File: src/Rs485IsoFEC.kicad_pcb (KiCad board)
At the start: 2 copper layers, 24 x 27.9 mm, 28 parts, among them J1 B4B-XH-A, P1 105444-0001, Q1 DMP3099L-13, U1 FT232RL, U2 ADM2682E

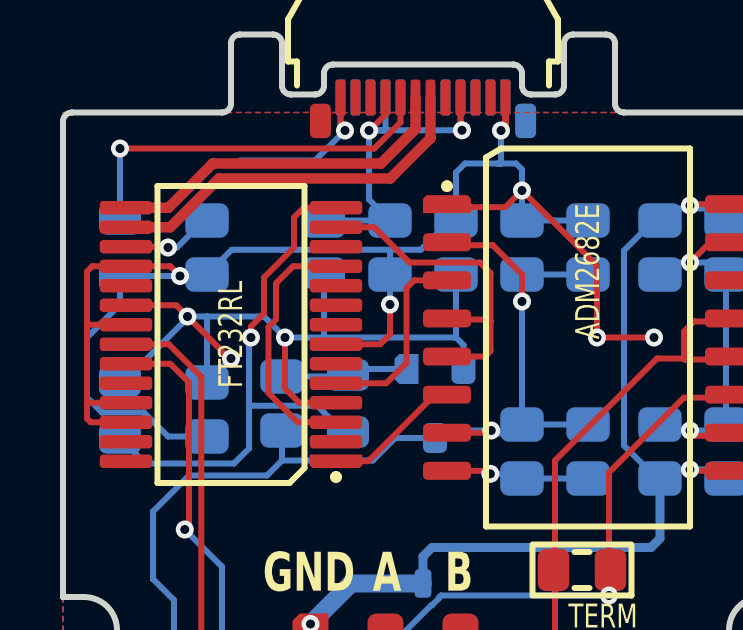
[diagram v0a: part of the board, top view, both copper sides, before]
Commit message: Removed internal RTS/CTS connection
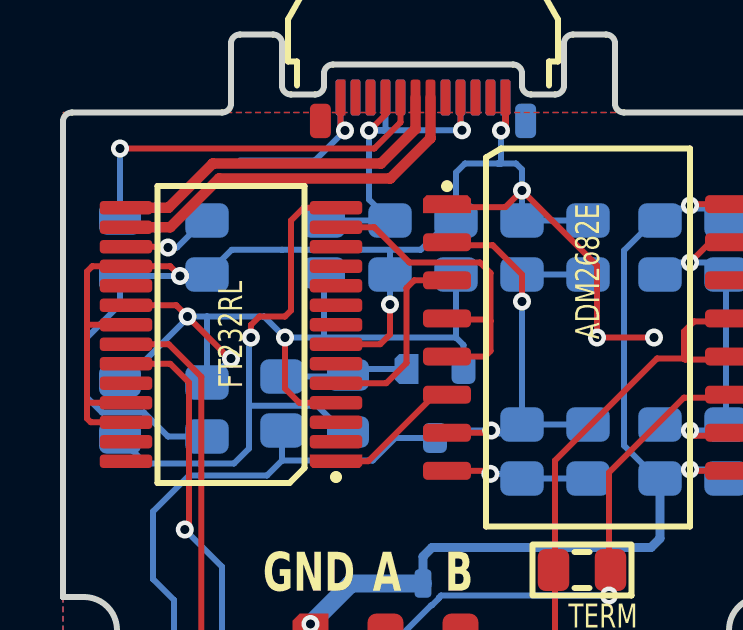
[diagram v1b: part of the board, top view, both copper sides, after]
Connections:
- U1 pad 11: RTS_CTS -> (no net)
- U1 pad 3: RTS_CTS -> (no net)
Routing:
- net RTS_CTS: track 8.65 -> 0.00 mm

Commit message: Updated connector to solder all 4 pins
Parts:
- R1: value TERM -> 120R
- moved R1 2.79 mm to (39.3, 39.8), turned to -90 degrees
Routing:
- net ISO_B: track 23.0 -> 24.7 mm
- net GND: track 72.4 -> 73.7 mm, vias 8 -> 9
- net ISO_A: track 24.3 -> 25.1 mm
- net 5V_SW: track 56.4 -> 56.3 mm, vias 3 -> 2
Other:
- board text added: "Rs485IsoFEC A"
- board text added: "TERM"
- board text removed: "Rs485IsoFEC B"

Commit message: Refactoring copper pour
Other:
- rule pad_to_mask_clearance: 0 -> 0.05
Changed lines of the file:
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@@
       (dielectric_constraints no)
     )
-    (pad_to_mask_clearance 0)
+    (pad_to_mask_clearance 0.05)
     (aux_axis_origin 20 20)
     (pcbplotparams
@@
         (effects (font (size 0.13 0.07) (thickness 0.01) bold))
     )
+    (fp_text user "D" (at 0 0.5) (layer "Cmts.User" knockout)
+        (effects (font (size 0.13 0.07) (thickness 0.01) bold))
+    )
     (fp_text user "G" (at -0.95 -0.5) (layer "Cmts.User" knockout)
         (effects (font (size 0.13 0.07) (thickness 0.01) bold))
     )
-    (fp_text user "D" (at 0 0.5) (layer "Cmts.User" knockout)
-        (effects (font (size 0.13 0.07) (thickness 0.01) bold))
-    )
     (fp_rect (start -1.35 0.25) (end 1.35 -0.25)
       (stroke (width 0.2) (type default)) (fill none) (layer "B.SilkS"))
-    (fp_circle (center -1.575 -1.15) (end -1.425 -1.15)
+    (fp_circle (center -1.65 -1.15) (end -1.5 -1.15)
       (stroke (width 0.1) (type solid)) (fill solid) (layer "B.SilkS"))
     (fp_rect (start -1.75 1.95) (end 1.75 -1.95)
@@
   (segment (start 32.95 40.25) (end 33.3 40.6) (width 0.2) (layer "B.Cu") (net 21))
   (zone (net 7) (net_name "GND") (layers "F&B.Cu") (hatch edge 0.5)
-    (connect_pads (clearance 0.25))
-    (min_thickness 0.25) (filled_areas_thickness no)
+    (connect_pads no (clearance 0.3))
+    (min_thickness 0.3) (filled_areas_thickness no)
     (fill yes (thermal_gap 0.5) (thermal_bridge_width 0.5))
     (polygon
